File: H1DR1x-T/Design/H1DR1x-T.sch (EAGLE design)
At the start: 32 parts, among them P1 HEXABIT_17.32_NO_P6, P2 RS-485, U1 STM32F091CBU6, U2 MAX14840EASAT, X1 XTALL_CSTCE8M00G52

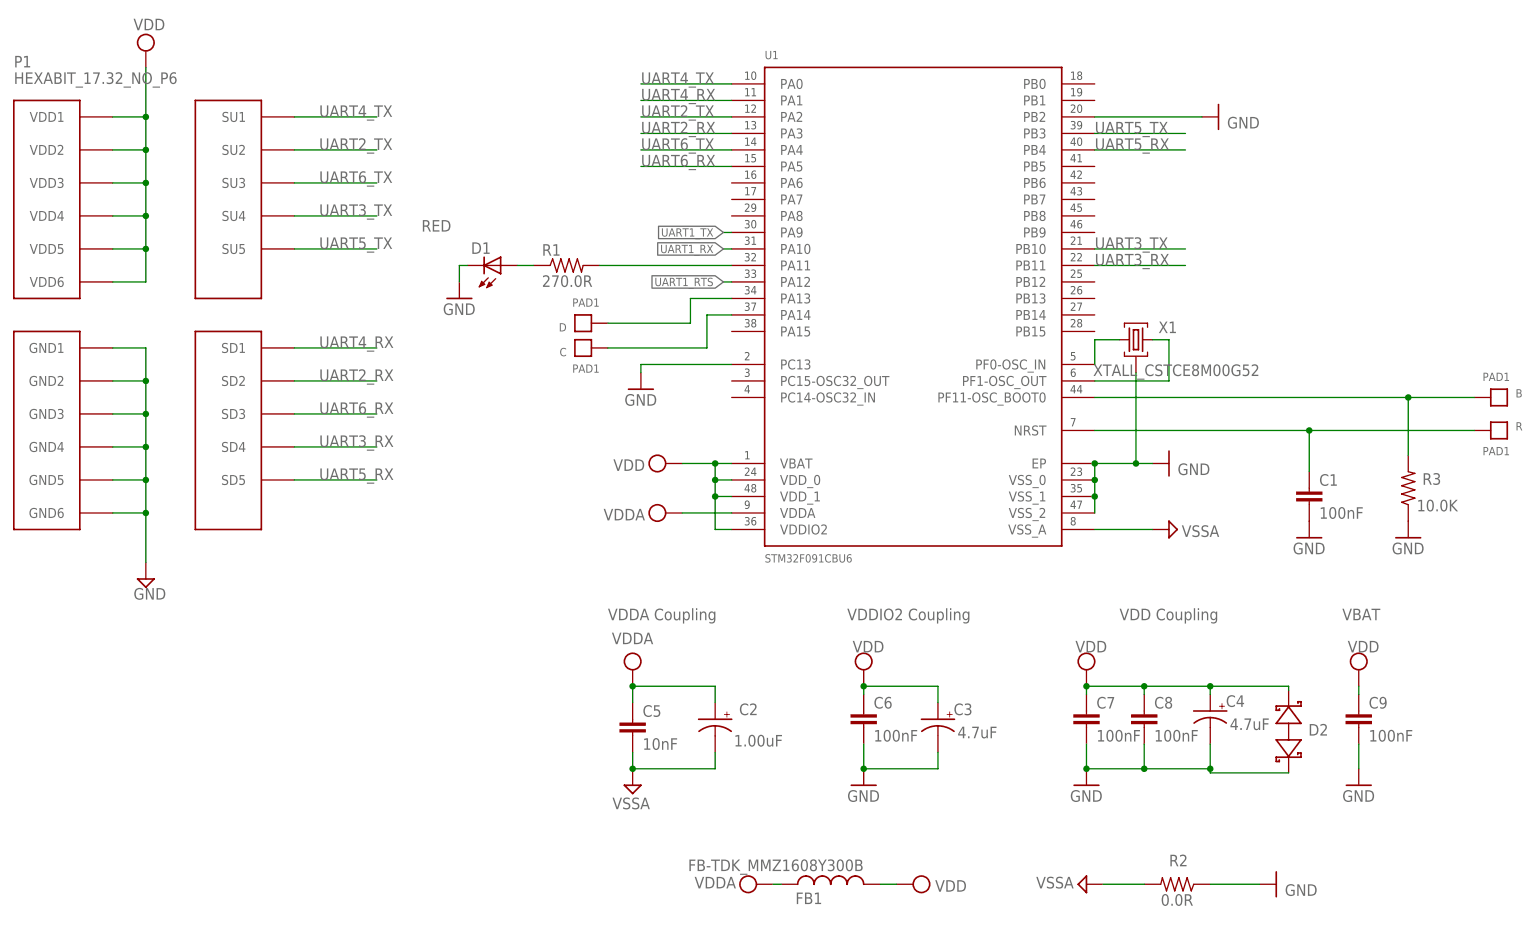
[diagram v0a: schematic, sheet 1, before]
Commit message: - Renamed files to H1DR1x-T. - Deleted Gerber and Drill files.
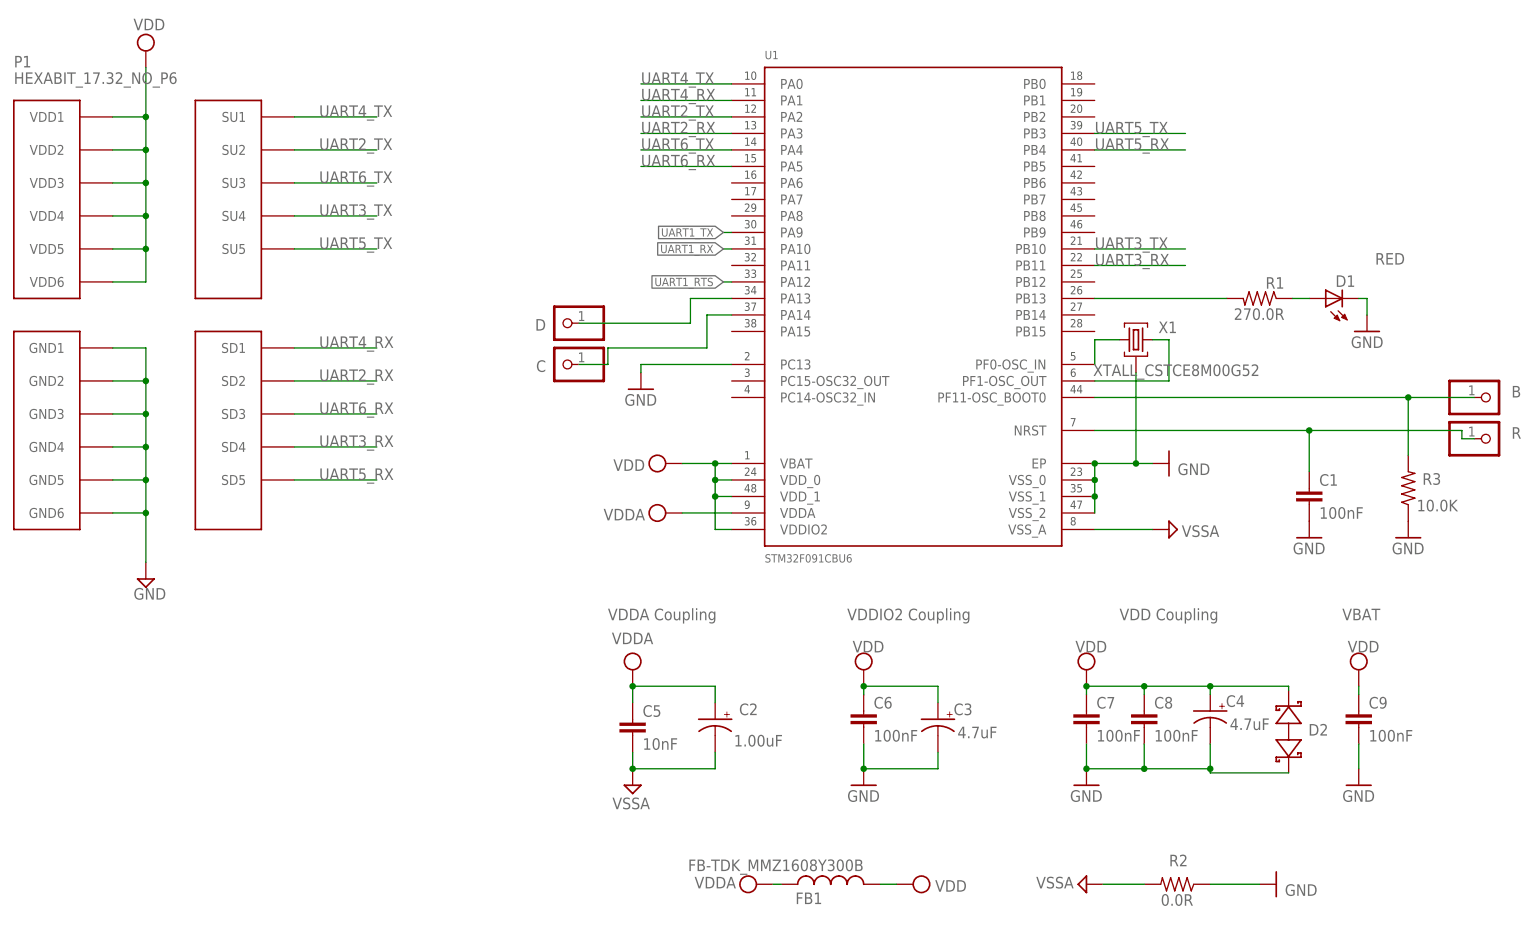
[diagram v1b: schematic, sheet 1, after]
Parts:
- B, C, D, R: value PAD1 -> (none); device Hexabitz:PAD1 -> HEXABITZ_USER_INTERFACE_PARTS:PINHD-1X1
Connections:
- net B1: now also B.1; no longer B.P$1
- net GND: no longer U1.PB2
- net N$1: now also D.1; no longer D.P$1
- net N$3: now also U1.PB13; no longer U1.PA11
- net N$9: now also C.1; no longer C.P$1
- net R1: now also R.1; no longer R.P$1
- net UART1_RX: now also U2.RO; no longer U2.DI
- net UART1_TX: now also U2.DI; no longer U2.RO
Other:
- moved on the sheet: D1, R1
